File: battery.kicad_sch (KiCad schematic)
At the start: 40 parts, among them J3 Lipo, Q2 AO3401A, Q3 IRLZ44N, Q4 IRLZ44N, Q5 2N7002, SW2 SW_Push, SW4 SW_SPST, U2 BQ76920PW

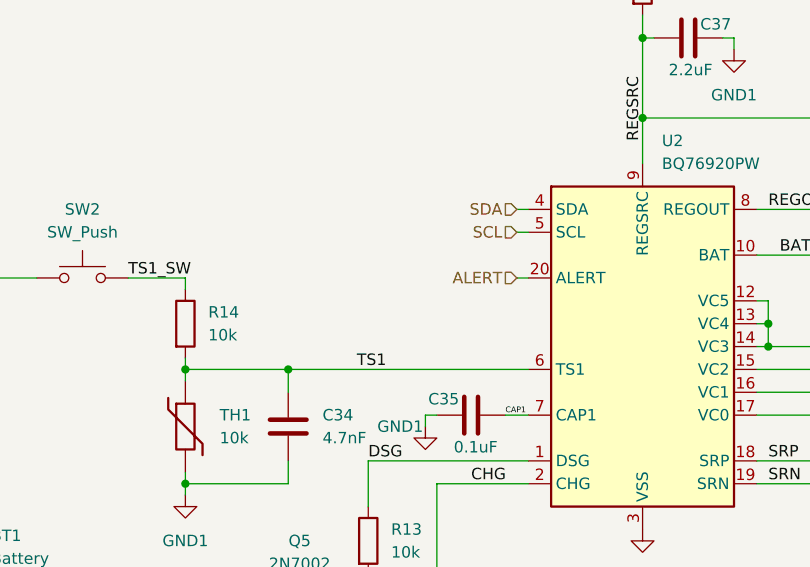
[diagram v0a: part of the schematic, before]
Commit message: connected some unconnected pins
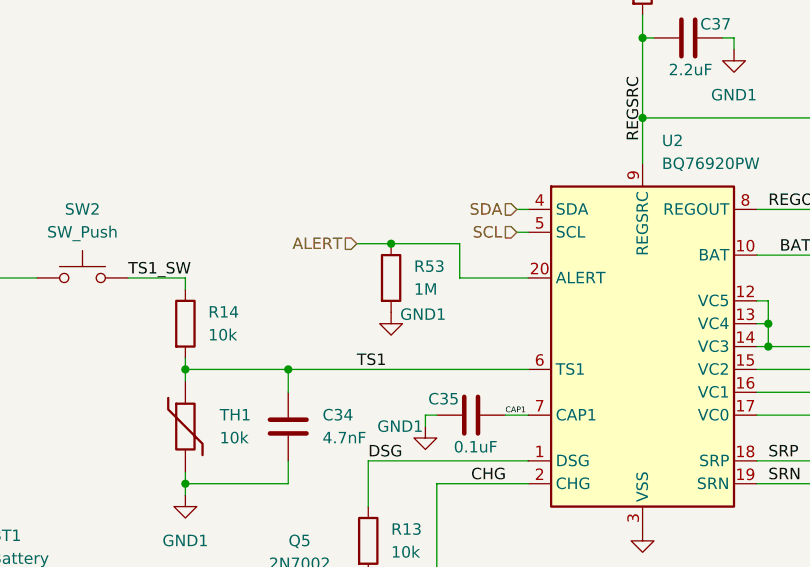
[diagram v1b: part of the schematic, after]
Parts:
- added R53: 1M, Resistor_SMD:R_0402_1005Metric, symbol Device:R
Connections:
- net ALERT: now also R53.1
- net GND1: now also R53.2
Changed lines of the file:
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@@
 	)
 	(junction
+		(at 138.43 73.66)
+		(diameter 0)
+		(color 0 0 0 0)
+	)
+	(junction
 		(at 167.64 133.35)
 		(diameter 0)
@@
 	(wire
 		(pts
+			(xy 146.05 73.66) (xy 146.05 77.47)
+		)
+		(stroke
+			(width 0)
+			(type default)
+		)
+	)
+	(wire
+		(pts
 			(xy 185.42 143.51) (xy 190.5 143.51)
 		)
@@
 	(wire
 		(pts
-			(xy 152.4 77.47) (xy 153.67 77.47)
+			(xy 134.62 73.66) (xy 138.43 73.66)
 		)
 		(stroke
@@
 	(wire
 		(pts
+			(xy 138.43 73.66) (xy 146.05 73.66)
+		)
+		(stroke
+			(width 0)
+			(type default)
+		)
+	)
+	(wire
+		(pts
 			(xy 166.37 39.37) (xy 166.37 40.64)
 		)
@@
 	(wire
 		(pts
+			(xy 146.05 77.47) (xy 153.67 77.47)
+		)
+		(stroke
+			(width 0)
+			(type default)
+		)
+	)
+	(wire
+		(pts
 			(xy 115.57 100.33) (xy 115.57 101.6)
 		)
@@
 	(hierarchical_label "ALERT"
 		(shape input)
-		(at 152.4 77.47 180)
+		(at 134.62 73.66 180)
 		(effects
 			(font
@@
 	)
 	(symbol
+		(lib_id "power:GND1")
+		(at 138.43 81.28 0)
+		(unit 1)
+		(exclude_from_sim no)
+		(in_bom yes)
+		(on_board yes)
+		(dnp no)
+		(property "Reference" "#PWR0100"
+			(at 138.43 87.63 0)
+			(effects
+				(font
+					(size 1.27 1.27)
+				)
+				(hide yes)
+			)
+		)
+		(property "Value" "GND1"
+			(at 141.986 81.534 0)
+			(effects
+				(font
+					(size 1.27 1.27)
+				)
+			)
+		)
+		(property "Footprint" ""
+			(at 138.43 81.28 0)
+			(effects
+				(font
+					(size 1.27 1.27)
+				)
+				(hide yes)
+			)
+		)
+		(property "Datasheet" ""
+			(at 138.43 81.28 0)
+			(effects
+				(font
+					(size 1.27 1.27)
+				)
+				(hide yes)
+			)
+		)
+		(property "Description" "Power symbol creates a global label with name \"GND1\" , ground"
+			(at 138.43 81.28 0)
+			(effects
+				(font
+					(size 1.27 1.27)
+				)
+				(hide yes)
+			)
+		)
+		(pin "1"
+		)
+		(instances
+			(project "robot_pcb"
+				(path "/2f56b371-1597-47e1-a48d-b7f69d342f77/8e993949-53ac-4d46-9f7d-59c9cf3d33c4"
+					(reference "#PWR0100")
+					(unit 1)
+				)
+			)
+		)
+	)
+	(symbol
 		(lib_id "Device:R")
 		(at 194.31 143.51 90)
@@
 					(unit 1)
 				)
+			)
+		)
+	)
+	(symbol
+		(lib_id "Device:R")
+		(at 138.43 77.47 0)
+		(unit 1)
+		(exclude_from_sim no)
+		(in_bom yes)
+		(on_board yes)
+		(dnp no)
+		(fields_autoplaced yes)
+		(property "Reference" "R53"
+			(at 140.97 76.1999 0)
+			(effects
+				(font
+					(size 1.27 1.27)
+				)
+				(justify left)
+			)
+		)
+		(property "Value" "1M"
+			(at 140.97 78.7399 0)
+			(effects
+				(font
+					(size 1.27 1.27)
+				)
+				(justify left)
+			)
+		)
+		(property "Footprint" "Resistor_SMD:R_0402_1005Metric"
+			(at 136.652 77.47 90)
+			(effects
+				(font
+					(size 1.27 1.27)
+				)
+				(hide yes)
+			)
+		)
+		(property "Datasheet" "~"
+			(at 138.43 77.47 0)
+			(effects
+				(font
+					(size 1.27 1.27)
+				)
+				(hide yes)
+			)
+		)
+		(property "Description" "Resistor"
+			(at 138.43 77.47 0)
+			(effects
+				(font
+					(size 1.27 1.27)
+				)
+				(hide yes)
+			)
+		)
+		(pin "1"
+		)
+		(pin "2"
+		)
+		(instances
+			(project ""
+				(path "/2f56b371-1597-47e1-a48d-b7f69d342f77/8e993949-53ac-4d46-9f7d-59c9cf3d33c4"
+					(reference "R53")
+					(unit 1)
+				)

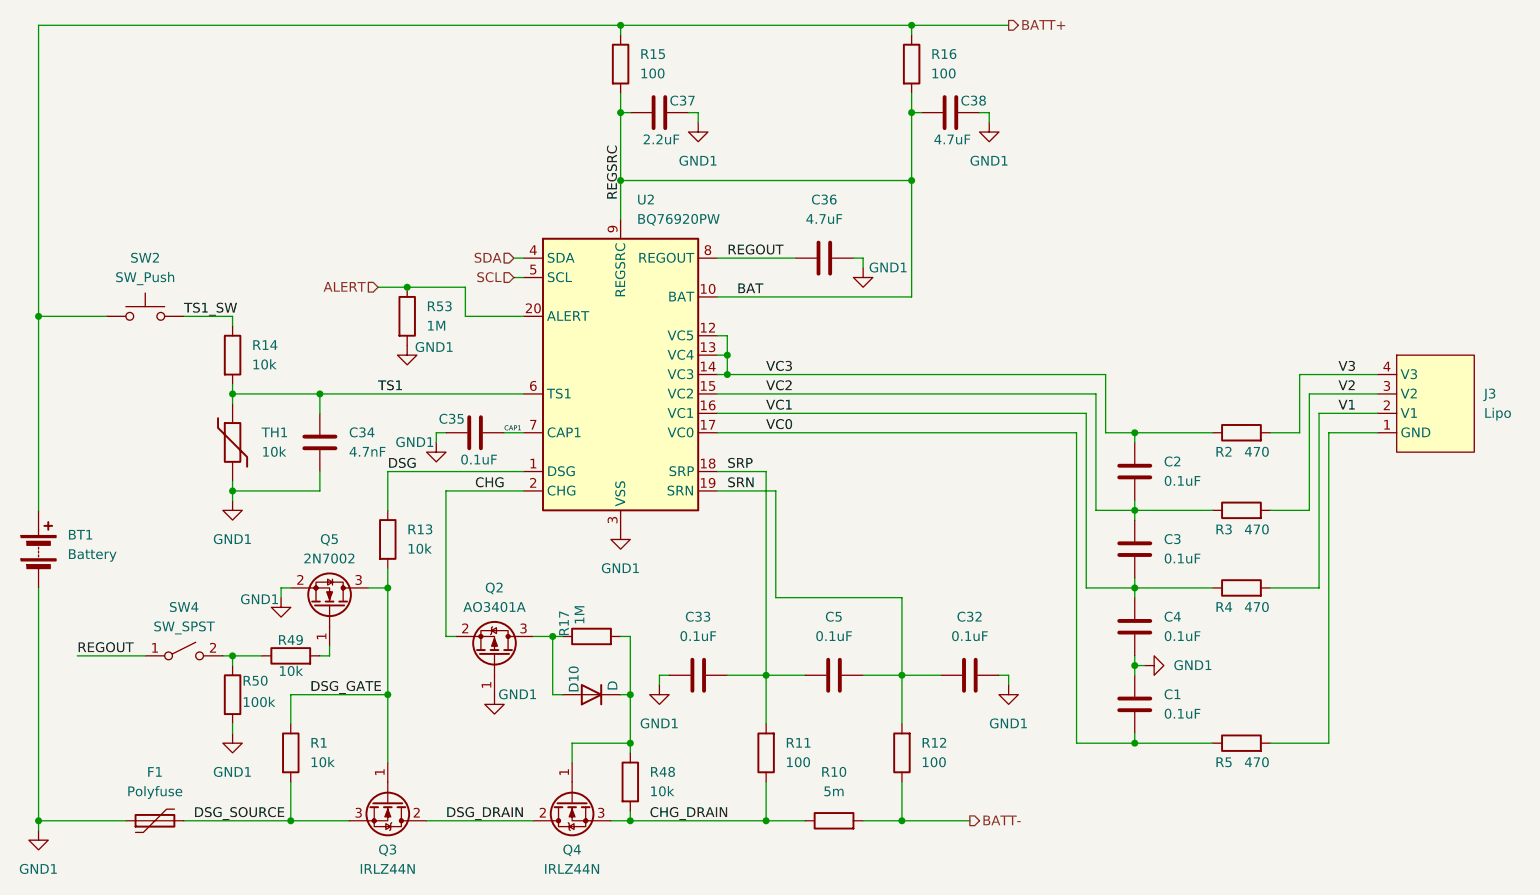
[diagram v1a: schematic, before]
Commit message: Update battery.kicad_sch
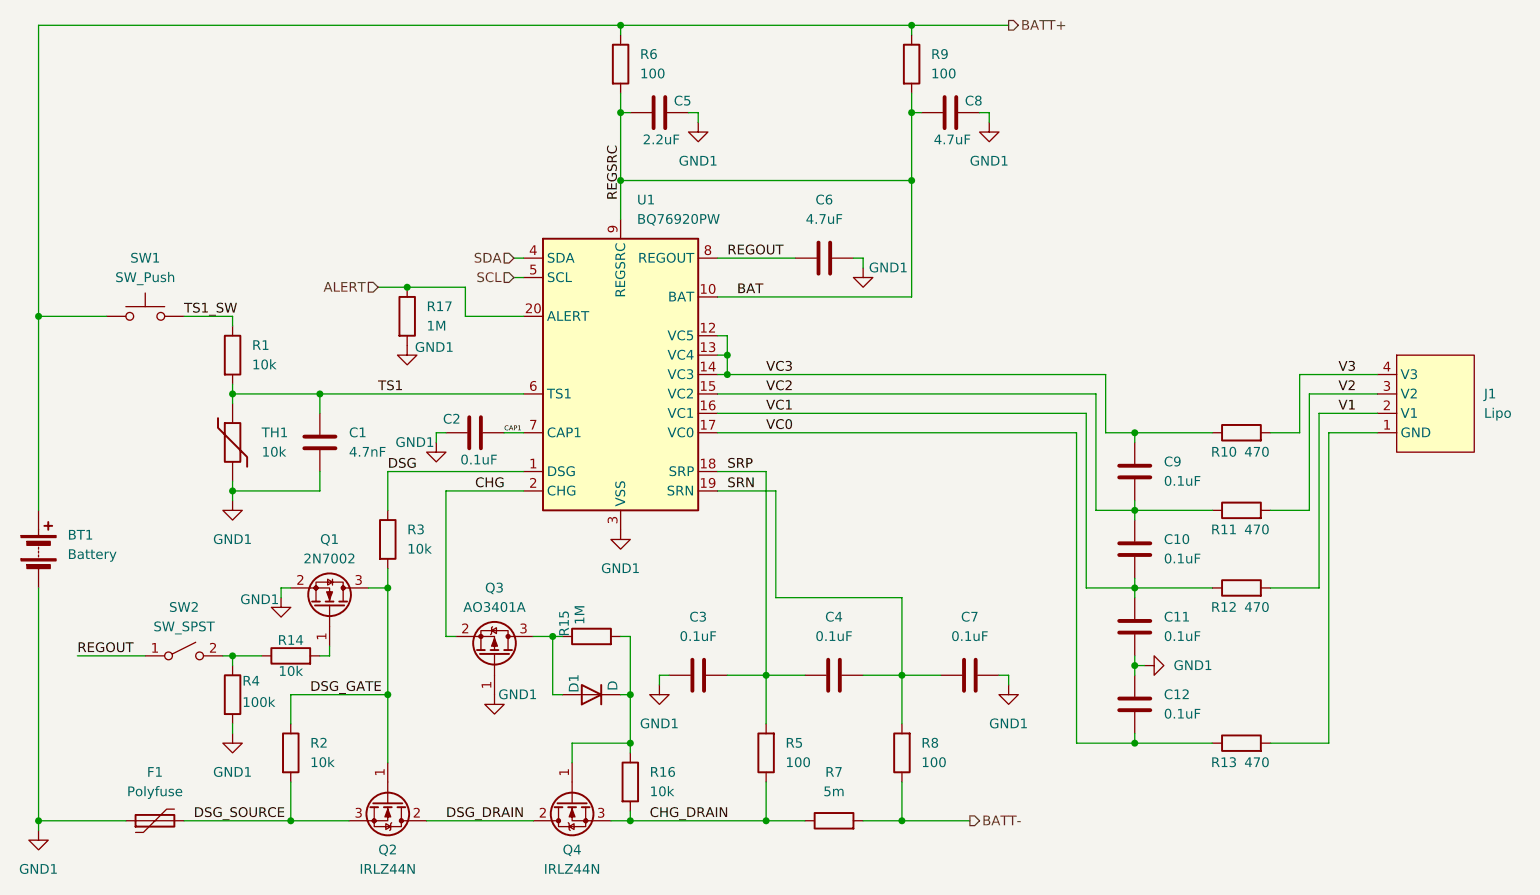
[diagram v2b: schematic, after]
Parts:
- renumbered C34 to C1, C3 to C10, C4 to C11, C1 to C12, C35 to C2, C33 to C3, C5 to C4, C37 to C5, C36 to C6, C32 to C7, C38 to C8, C2 to C9, D10 to D1, J3 to J1, Q5 to Q1, Q3 to Q2, Q2 to Q3, R14 to R1, R2 to R10, R3 to R11, R4 to R12, R5 to R13, R49 to R14, R17 to R15, R48 to R16, R53 to R17, R1 to R2, R13 to R3, R50 to R4, R11 to R5, R15 to R6, R10 to R7, R12 to R8, R16 to R9, SW2 to SW1, SW4 to SW2, U2 to U1
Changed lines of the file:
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@@
 		(dnp no)
 		(fields_autoplaced yes)
-		(property "Reference" "SW4"
+		(property "Reference" "SW2"
 			(at 109.22 115.57 0)
 			(effects
@@
 		(dnp no)
 		(fields_autoplaced yes)
-		(property "Reference" "R14"
+		(property "Reference" "R1"
 			(at 118.11 81.2799 0)
 			(effects
@@
 		(dnp no)
 		(fields_autoplaced yes)
-		(property "Reference" "R12"
+		(property "Reference" "R8"
 			(at 205.74 133.3499 0)
 			(effects
@@
 		(dnp no)
 		(fields_autoplaced yes)
-		(property "Reference" "C5"
+		(property "Reference" "C4"
 			(at 194.31 116.84 90)
 			(effects
@@
 		(on_board yes)
 		(dnp no)
-		(property "Reference" "#PWR072"
+		(property "Reference" "#PWR013"
 			(at 121.92 120.65 0)
 			(effects
@@
 		(on_board yes)
 		(dnp no)
-		(property "Reference" "R5"
+		(property "Reference" "R13"
 			(at 245.364 135.89 90)
 			(effects
@@
 		(on_board yes)
 		(dnp no)
-		(property "Reference" "D10"
+		(property "Reference" "D1"
 			(at 160.274 126.746 90)
 			(effects
@@
 		(on_board yes)
 		(dnp no)
-		(property "Reference" "Q2"
+		(property "Reference" "Q3"
 			(at 149.86 113.03 90)
 			(effects
@@
 		(dnp no)
 		(fields_autoplaced yes)
-		(property "Reference" "C34"
+		(property "Reference" "C1"
 			(at 130.81 92.7099 0)
 			(effects
@@
 		(dnp no)
 		(fields_autoplaced yes)
-		(property "Reference" "#PWR034"
+		(property "Reference" "#PWR07"
 			(at 176.53 58.42 0)
 			(effects
@@
 		(on_board yes)
 		(dnp no)
-		(property "Reference" "#PWR028"
+		(property "Reference" "#PWR04"
 			(at 149.86 133.35 0)
 			(effects
@@
 		(dnp no)
 		(fields_autoplaced yes)
-		(property "Reference" "R48"
+		(property "Reference" "R16"
 			(at 170.18 137.1599 0)
 			(effects
@@
 		(dnp no)
 		(fields_autoplaced yes)
-		(property "Reference" "C3"
+		(property "Reference" "C10"
 			(at 237.49 106.6799 0)
 			(effects
@@
 		(dnp no)
 		(fields_autoplaced yes)
-		(property "Reference" "#PWR029"
+		(property "Reference" "#PWR05"
 			(at 171.45 132.08 0)
 			(effects
@@
 		(dnp no)
 		(fields_autoplaced yes)
-		(property "Reference" "C33"
+		(property "Reference" "C3"
 			(at 176.53 116.84 90)
 			(effects
@@
 		(dnp no)
 		(fields_autoplaced yes)
-		(property "Reference" "#PWR04"
+		(property "Reference" "#PWR02"
 			(at 115.57 107.95 0)
 			(effects
@@
 		(dnp no)
 		(fields_autoplaced yes)
-		(property "Reference" "R15"
+		(property "Reference" "R6"
 			(at 168.91 43.1799 0)
 			(effects
@@
 		(dnp no)
 		(fields_autoplaced yes)
-		(property "Reference" "U2"
+		(property "Reference" "U1"
 			(at 168.5133 62.23 0)
 			(effects
@@
 		(dnp no)
 		(fields_autoplaced yes)
-		(property "Reference" "C36"
+		(property "Reference" "C6"
 			(at 193.04 62.23 90)
 			(effects
@@
 		(on_board yes)
 		(dnp no)
-		(property "Reference" "#PWR0100"
+		(property "Reference" "#PWR014"
 			(at 138.43 87.63 0)
 			(effects
@@
 				)
 			)
+			(project "battery"
+				(path "/5852dc9c-be81-4731-9c95-5e6ebdb17894"
+					(reference "#PWR014")
+					(unit 1)
+				)
+			)
 		)
 	)
@@
 		(dnp no)
 		(fields_autoplaced yes)
-		(property "Reference" "R10"
+		(property "Reference" "R7"
 			(at 194.31 137.16 90)
 			(effects
@@
 		(dnp no)
 		(fields_autoplaced yes)
-		(property "Reference" "#PWR073"
+		(property "Reference" "#PWR012"
 			(at 115.57 138.43 0)
 			(effects
@@
 		(dnp no)
 		(fields_autoplaced yes)
-		(property "Reference" "#PWR033"
+		(property "Reference" "#PWR010"
 			(at 214.63 58.42 0)
 			(effects
@@
 		(dnp no)
 		(fields_autoplaced yes)
-		(property "Reference" "Q3"
+		(property "Reference" "Q2"
 			(at 135.89 147.32 90)
 			(effects
@@
 		(dnp no)
 		(fields_autoplaced yes)
-		(property "Reference" "R1"
+		(property "Reference" "R2"
 			(at 125.73 133.3499 0)
 			(effects
@@
 		(on_board yes)
 		(dnp no)
-		(property "Reference" "Q5"
+		(property "Reference" "Q1"
 			(at 128.27 106.68 90)
 			(effects
@@
 		(dnp no)
 		(fields_autoplaced yes)
-		(property "Reference" "#PWR03"
+		(property "Reference" "#PWR01"
 			(at 90.17 151.13 0)
 			(effects
@@
 		(dnp no)
 		(fields_autoplaced yes)
-		(property "Reference" "R11"
+		(property "Reference" "R5"
 			(at 187.96 133.3499 0)
 			(effects
@@
 		(dnp no)
 		(fields_autoplaced yes)
-		(property "Reference" "#PWR031"
+		(property "Reference" "#PWR011"
 			(at 241.3 123.19 0)
 			(effects
@@
 		(dnp no)
 		(fields_autoplaced yes)
-		(property "Reference" "C2"
+		(property "Reference" "C9"
 			(at 237.49 96.5199 0)
 			(effects
@@
 		(dnp no)
 		(fields_autoplaced yes)
-		(property "Reference" "C1"
+		(property "Reference" "C12"
 			(at 237.49 126.9999 0)
 			(effects
@@
 		(on_board yes)
 		(dnp no)
-		(property "Reference" "R50"
+		(property "Reference" "R4"
 			(at 116.84 125.222 0)
 			(effects
@@
 		(on_board yes)
 		(dnp no)
-		(property "Reference" "#PWR035"
+		(property "Reference" "#PWR03"
 			(at 142.24 100.33 0)
 			(effects
@@
 		(on_board yes)
 		(dnp no)
-		(property "Reference" "R17"
+		(property "Reference" "R15"
 			(at 159.004 119.38 0)
 			(effects
@@
 		(on_board yes)
 		(dnp no)
-		(property "Reference" "#PWR032"
+		(property "Reference" "#PWR08"
 			(at 198.12 77.47 0)
 			(effects
@@
 		(dnp no)
 		(fields_autoplaced yes)
-		(property "Reference" "SW2"
+		(property "Reference" "SW1"
 			(at 104.14 69.85 0)
 			(effects
@@
 		(dnp no)
 		(fields_autoplaced yes)
-		(property "Reference" "J3"
+		(property "Reference" "J1"
 			(at 279.4 87.6299 0)
 			(effects
@@
 		(on_board yes)
 		(dnp no)
-		(property "Reference" "R2"
+		(property "Reference" "R10"
 			(at 245.364 95.25 90)
 			(effects
@@
 		(on_board yes)
 		(dnp no)
-		(property "Reference" "R4"
+		(property "Reference" "R12"
 			(at 245.364 115.57 90)
 			(effects
@@
 		(dnp no)
 		(fields_autoplaced yes)
-		(property "Reference" "R53"
+		(property "Reference" "R17"
 			(at 140.97 76.1999 0)
 			(effects
@@
 				)
 			)
+			(project "battery"
+				(path "/5852dc9c-be81-4731-9c95-5e6ebdb17894"
+					(reference "R17")
+					(unit 1)
+				)
+			)
 		)
 	)
@@
 		(dnp no)
 		(fields_autoplaced yes)
-		(property "Reference" "C32"
+		(property "Reference" "C7"
 			(at 212.09 116.84 90)
 			(effects
@@
 		(dnp no)
 		(fields_autoplaced yes)
-		(property "Reference" "C4"
+		(property "Reference" "C11"
 			(at 237.49 116.8399 0)
 			(effects
@@
 		(on_board yes)
 		(dnp no)
-		(property "Reference" "C35"
+		(property "Reference" "C2"
 			(at 144.272 90.932 90)
 			(effects
@@
 		(on_board yes)
 		(dnp no)
-		(property "Reference" "C38"
+		(property "Reference" "C8"
 			(at 212.598 49.276 90)
 			(effects
@@
 		(on_board yes)
 		(dnp no)
-		(property "Reference" "R49"
+		(property "Reference" "R14"
 			(at 123.19 119.888 90)
 			(effects
@@
 		(on_board yes)
 		(dnp no)
-		(property "Reference" "C37"
+		(property "Reference" "C5"
 			(at 174.498 49.276 90)
 			(effects
@@
 		(on_board yes)
 		(dnp no)
-		(property "Reference" "R3"
+		(property "Reference" "R11"
 			(at 245.364 105.41 90)
 			(effects
@@
 		(dnp no)
 		(fields_autoplaced yes)
-		(property "Reference" "R13"
+		(property "Reference" "R3"
 			(at 138.43 105.4099 0)
 			(effects
@@
 		(dnp no)
 		(fields_autoplaced yes)
-		(property "Reference" "R16"
+		(property "Reference" "R9"
 			(at 207.01 43.1799 0)
 			(effects
@@
 		(dnp no)
 		(fields_autoplaced yes)
-		(property "Reference" "#PWR030"
+		(property "Reference" "#PWR09"
 			(at 217.17 132.08 0)
 			(effects
@@
 		(dnp no)
 		(fields_autoplaced yes)
-		(property "Reference" "#PWR05"
+		(property "Reference" "#PWR06"
 			(at 166.37 111.76 0)
 			(effects
